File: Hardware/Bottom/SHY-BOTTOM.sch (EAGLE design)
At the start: 31 parts, among them U1 AD5242-SO16

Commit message: bottom board design
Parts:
- added J1: (no value), LinnesLab-Connectors:CONN_07
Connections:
- removed net LED.CTRL: U$4.A
- removed net PPG: C21.2, OP3G$1.OUT, U1.B2
- removed net TIA: C10.2, C15.1, OP4G$1.OUT, U1.W1
- new net A6/TIA: C10.2, C15.1, J1.5, OP4G$1.OUT, U1.W1
- new net A7/PPG: C21.2, J1.7, OP3G$1.OUT, U1.B2
- new net D29/LED.CTRL: J1.6, U$4.A
- new net N$2: J1.4
- new net N$3: J1.3
- new net N$4: J1.2
- new net N$5: J1.1
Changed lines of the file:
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@@
 <part name="GND30" library="LinnesLab-Symbols" deviceset="GND" device=""/>
 <part name="SUPPLY24" library="LinnesLab-Symbols" deviceset="3.3V" device=""/>
+<part name="J1" library="LinnesLab-Connectors" deviceset="CONN_07" device=""/>
 </parts>
 <sheets>
@@
 <attribute name="VALUE" x="25.4" y="-22.606" size="1.778" layer="96" align="bottom-center"/>
 </instance>
+<instance part="J1" gate="G$1" x="137.16" y="-38.1" smashed="yes">
+<attribute name="VALUE" x="132.08" y="-48.006" size="1.778" layer="96" font="vector"/>
+<attribute name="NAME" x="132.08" y="-24.892" size="1.778" layer="95" font="vector"/>
+</instance>
 </instances>
 <busses>
@@
 </segment>
 </net>
-<net name="TIA" class="0">
+<net name="A6/TIA" class="0">
 <segment>
 <wire x1="142.24" y1="12.7" x2="137.16" y2="12.7" width="0.1524" layer="91"/>
@@
 <junction x="88.9" y="78.74"/>
 </segment>
+<segment>
+<pinref part="J1" gate="G$1" pin="5"/>
+<wire x1="142.24" y1="-33.02" x2="147.32" y2="-33.02" width="0.1524" layer="91"/>
+<label x="147.32" y="-33.02" size="1.27" layer="95" xref="yes"/>
+</segment>
 </net>
 <net name="PD.C" class="0">
@@
 </segment>
 </net>
-<net name="LED.CTRL" class="0">
+<net name="D29/LED.CTRL" class="0">
 <segment>
 <pinref part="U$4" gate="G$1" pin="A"/>
@@
 <wire x1="238.76" y1="15.24" x2="238.76" y2="22.86" width="0.1524" layer="91"/>
 <label x="238.76" y="22.86" size="1.27" layer="95" rot="R180" xref="yes"/>
+</segment>
+<segment>
+<pinref part="J1" gate="G$1" pin="6"/>
+<wire x1="142.24" y1="-30.48" x2="147.32" y2="-30.48" width="0.1524" layer="91"/>
+<label x="147.32" y="-30.48" size="1.27" layer="95" xref="yes"/>
 </segment>
 </net>
@@
 </segment>
 </net>
-<net name="PPG" class="0">
+<net name="A7/PPG" class="0">
 <segment>
 <wire x1="170.18" y1="12.7" x2="172.72" y2="12.7" width="0.1524" layer="91"/>
@@
 <label x="228.6" y="91.44" size="1.27" layer="95" rot="R180" xref="yes"/>
 <label x="228.6" y="71.12" size="1.27" layer="95" xref="yes"/>
+</segment>
+<segment>
+<pinref part="J1" gate="G$1" pin="7"/>
+<wire x1="142.24" y1="-27.94" x2="147.32" y2="-27.94" width="0.1524" layer="91"/>
+<label x="147.32" y="-27.94" size="1.27" layer="95" xref="yes"/>
 </segment>
 </net>
@@
 </segment>
 </net>
+<net name="N$2" class="0">
+<segment>
+<pinref part="J1" gate="G$1" pin="4"/>
+<wire x1="142.24" y1="-35.56" x2="147.32" y2="-35.56" width="0.1524" layer="91"/>
+</segment>
+</net>
+<net name="N$3" class="0">
+<segment>
+<pinref part="J1" gate="G$1" pin="3"/>
+<wire x1="142.24" y1="-38.1" x2="149.86" y2="-38.1" width="0.1524" layer="91"/>
+</segment>
+</net>
+<net name="N$4" class="0">
+<segment>
+<pinref part="J1" gate="G$1" pin="2"/>
+<wire x1="142.24" y1="-40.64" x2="149.86" y2="-40.64" width="0.1524" layer="91"/>
+</segment>
+</net>
+<net name="N$5" class="0">
+<segment>
+<pinref part="J1" gate="G$1" pin="1"/>
+<wire x1="142.24" y1="-43.18" x2="147.32" y2="-43.18" width="0.1524" layer="91"/>
+</segment>
+</net>

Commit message: till 53:17
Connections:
- removed net LED: Q1.C
- net LED.C: now also Q1.C
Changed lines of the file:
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@@
 <label x="43.18" y="78.74" size="1.27" layer="95" xref="yes"/>
+</segment>
+<segment>
+<wire x1="259.08" y1="15.24" x2="259.08" y2="17.78" width="0.1524" layer="91"/>
+<label x="259.08" y="17.78" size="1.27" layer="95" rot="R180" xref="yes"/>
+<pinref part="Q1" gate="G$1" pin="C"/>
 </segment>
 </net>
@@
 </segment>
 </net>
-<net name="LED" class="0">
-<segment>
-<wire x1="259.08" y1="15.24" x2="259.08" y2="17.78" width="0.1524" layer="91"/>
-<label x="259.08" y="17.78" size="1.27" layer="95" rot="R180" xref="yes"/>
-<pinref part="Q1" gate="G$1" pin="C"/>
-</segment>
-</net>

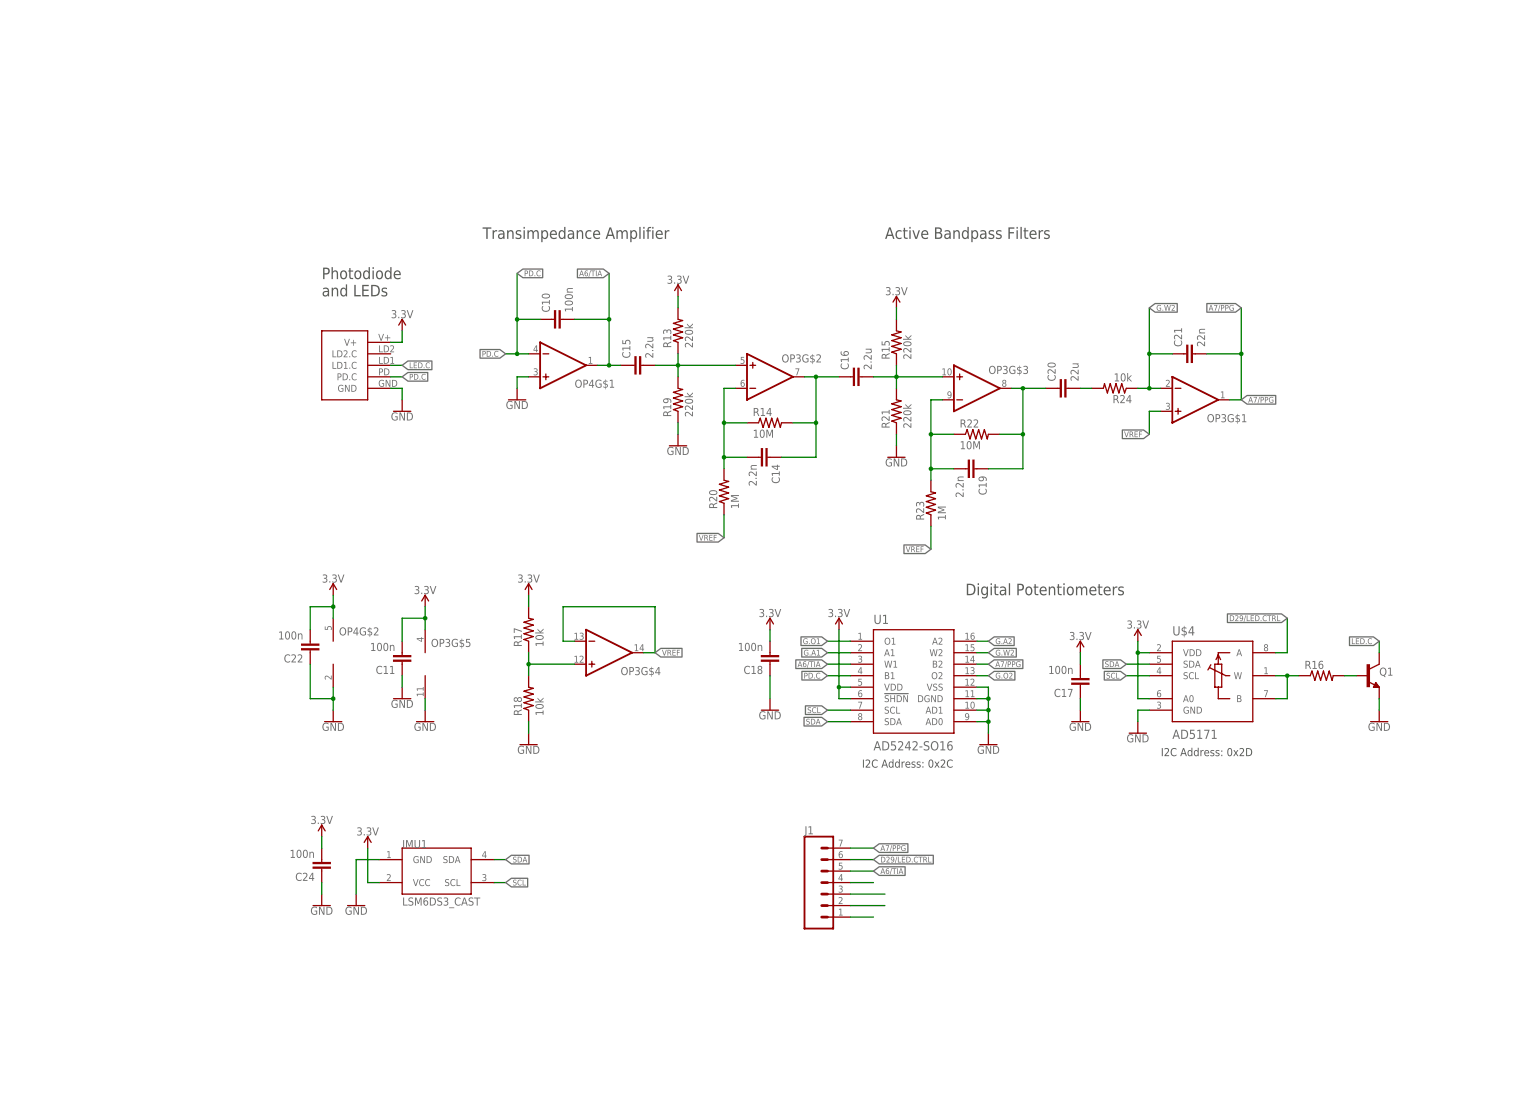
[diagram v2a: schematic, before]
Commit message: finish bottom board
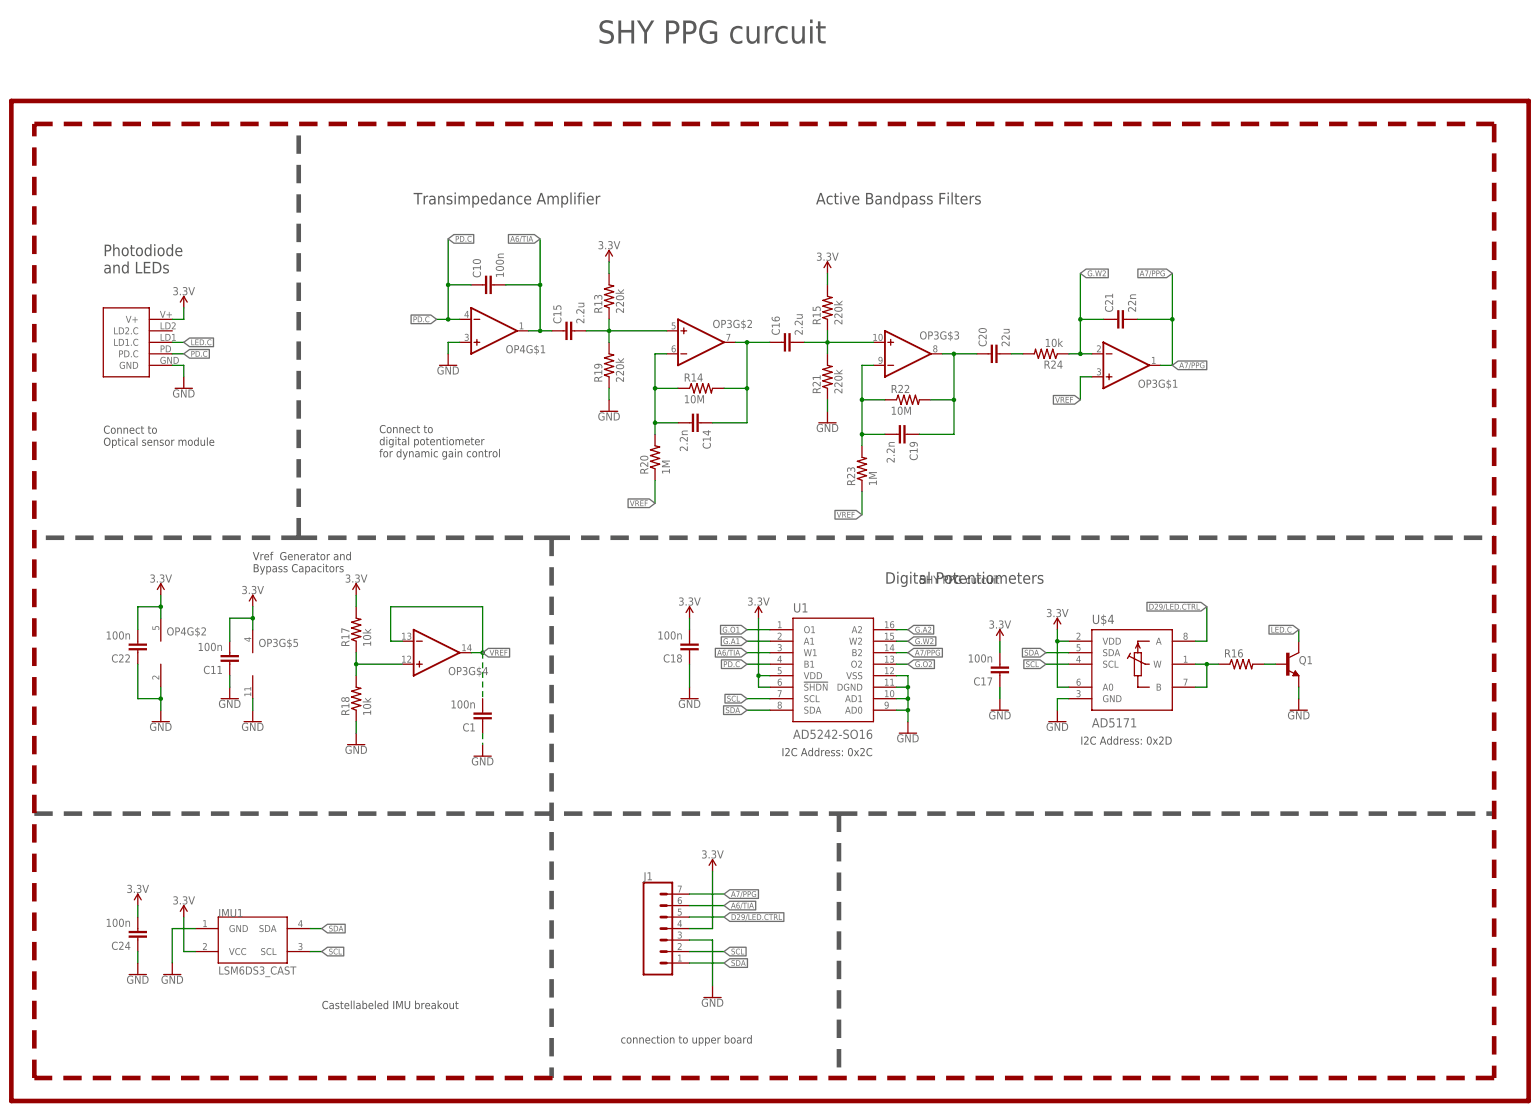
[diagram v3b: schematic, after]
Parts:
- added C1: 100n, LinnesLab-Passives:CAPACITOR0603
- added LOGO1: REVISION.A, LinnesLab-Logos:REVISION.A
- added LOGO2: LINNES.LAB.LOGO, LinnesLab-Logos:LINNES.LAB.LOGO
- J1: device LinnesLab-Connectors:CONN_07 -> LinnesLab-Connectors:CONN_07-1.27MM
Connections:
- removed net N$2: J1.4
- removed net N$3: J1.3
- removed net N$4: J1.2
- removed net N$5: J1.1
- net 3.3V: now also J1.4
- net A6/TIA: now also J1.6; no longer J1.5
- net D29/LED.CTRL: now also J1.5; no longer J1.6
- net GND: now also C1.1, J1.3
- net SCL: now also J1.2
- net SDA: now also J1.1
- net VREF: now also C1.2
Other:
- note added: "Castellabeled IMU breakout"
- note added: "Connect to Optical sensor module"
- note added: "Connect to digital potentiometer for dynamic gain control"
- note added: "SHY PPG curcuit"
- note added: "Vref Generator and Bypass Capacitors"
- note added: "connection to upper board"
- moved on the sheet: C10, C11, C14, C15, C16, C17, C18, C19, C20, C21, C22, C24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
